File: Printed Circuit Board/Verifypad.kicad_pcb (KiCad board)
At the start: 2 copper layers, 49 x 51.5 mm, 10 parts, among them J1 Conn_01x04, SW1 SW_Push, SW2 SW_Push, U1 MOUDLE-SEEEDUINO-XIAO

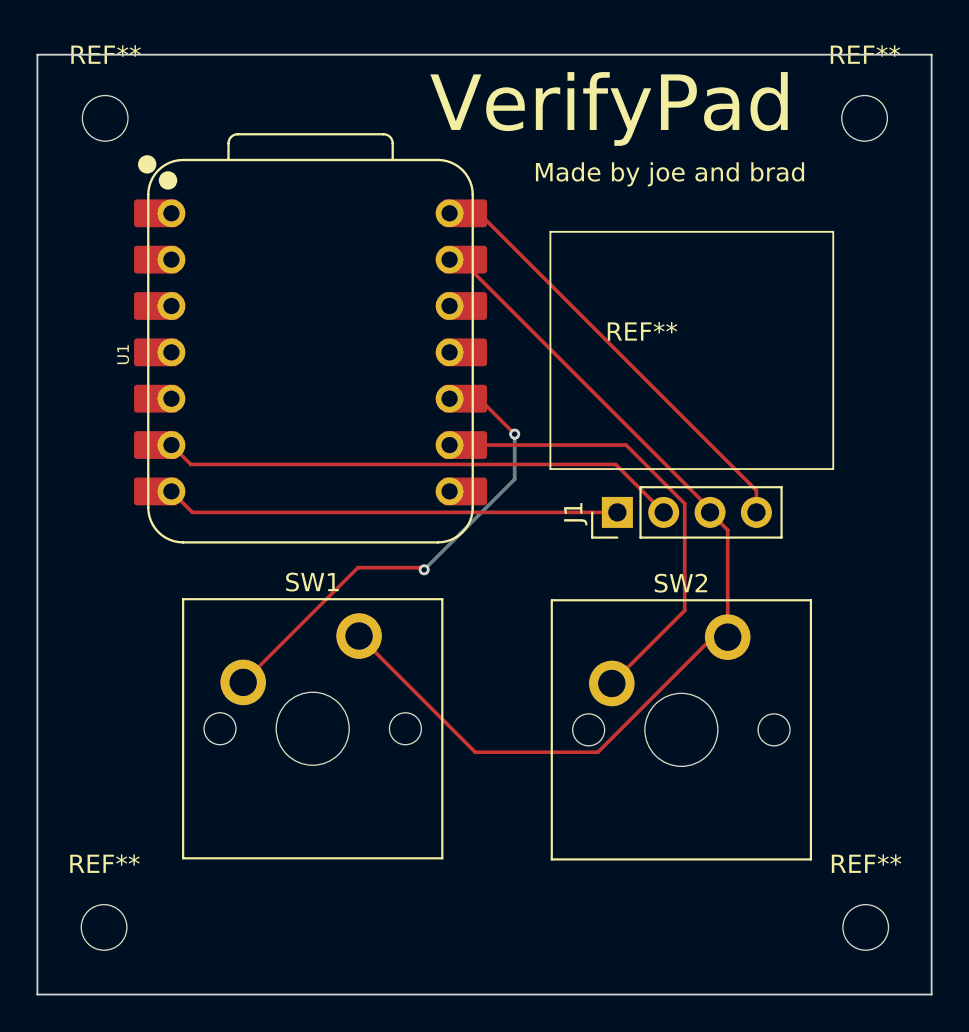
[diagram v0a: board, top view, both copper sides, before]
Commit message: added qr code to the pcb silkscreen
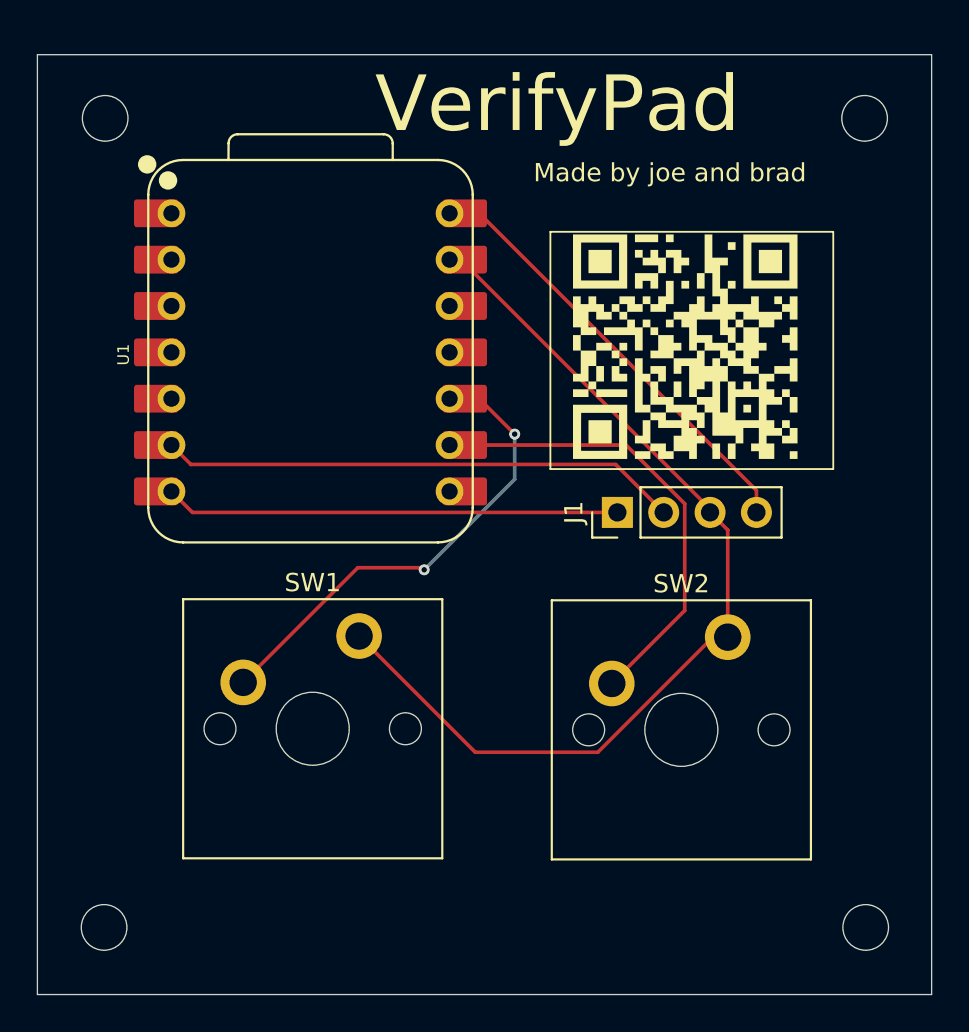
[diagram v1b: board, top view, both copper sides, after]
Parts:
- added G***: LOGO, LOGO, F.Cu at (196.0, 63.5)
- Waveshare 0.49" Display: renamed from REF**
